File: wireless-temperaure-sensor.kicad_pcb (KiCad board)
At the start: 2 copper layers, 45.1 x 55.9 mm, 18 parts, among them J1 Programmer, U1 stm32l010f4, U2 NRF24L01_Breakout, U3 MCP9808_MSOP

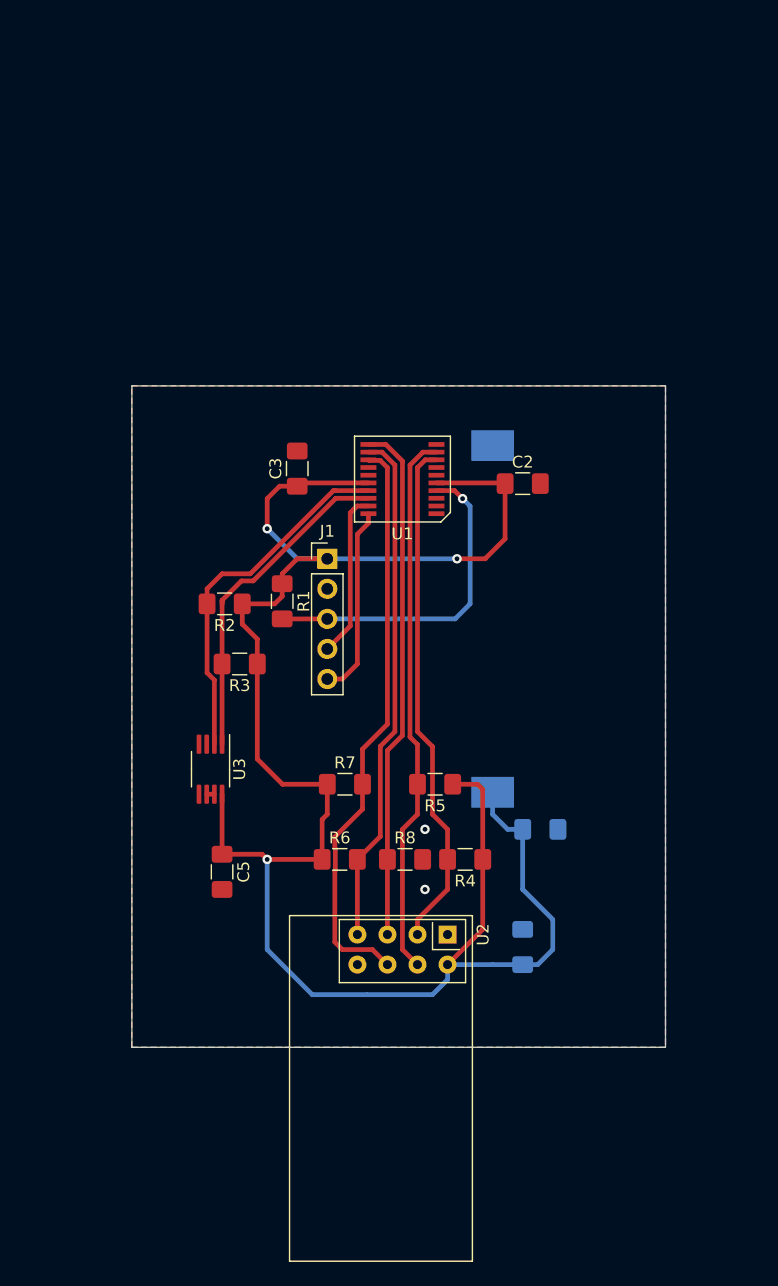
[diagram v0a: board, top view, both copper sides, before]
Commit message: Finished schematic and almost finished pcb
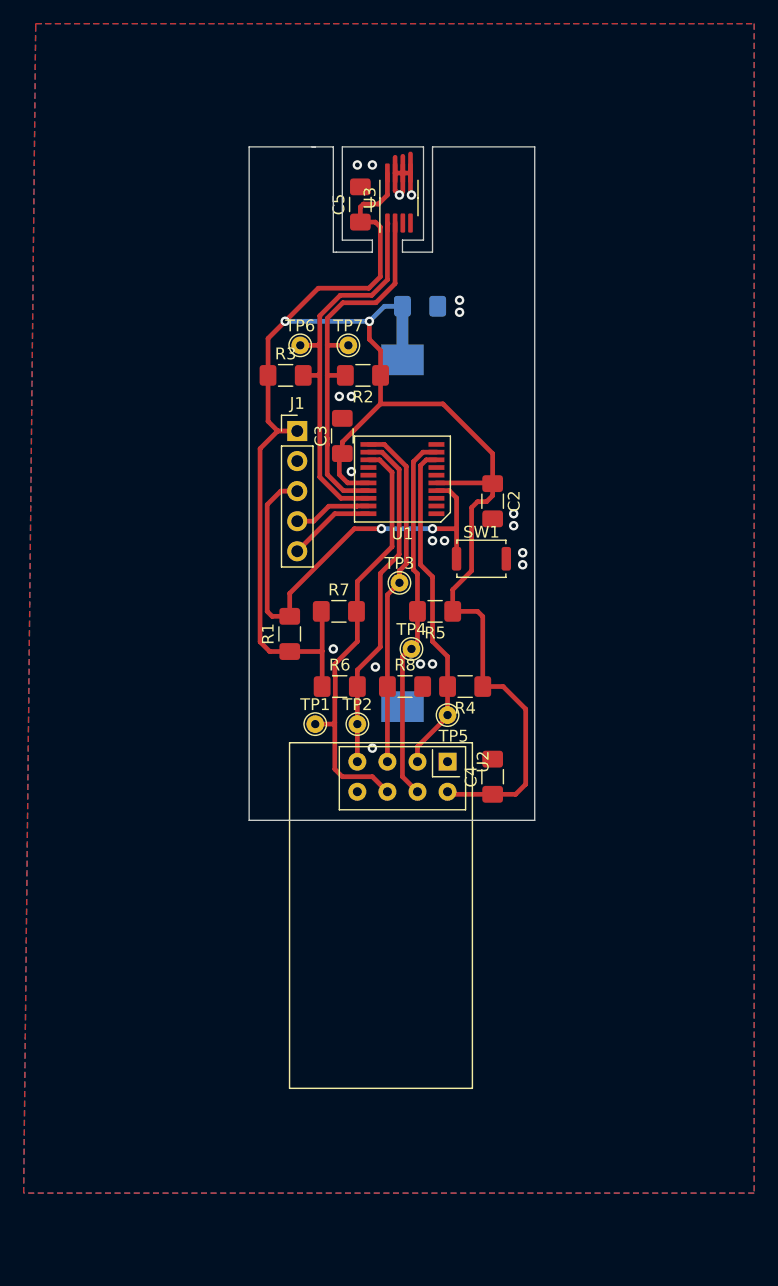
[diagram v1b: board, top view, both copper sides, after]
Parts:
- added SW1: SW_Push, Button_Switch_SMD:SW_Push_SPST_NO_Alps_SKRK, F.Cu at (105.7, 92.7)
- added TP1: , TestPoint:TestPoint_THTPad_D1.5mm_Drill0.7mm, F.Cu at (91.7, 106.7)
- added TP2: , TestPoint:TestPoint_THTPad_D1.5mm_Drill0.7mm, F.Cu at (95.2, 106.7)
- added TP3: , TestPoint:TestPoint_THTPad_D1.5mm_Drill0.7mm, F.Cu at (98.8, 94.7)
- added TP4: , TestPoint:TestPoint_THTPad_D1.5mm_Drill0.7mm, F.Cu at (99.8, 100.3)
- added TP5: , TestPoint:TestPoint_THTPad_D1.5mm_Drill0.7mm, F.Cu at (102.9, 105.9)
- added TP6: , TestPoint:TestPoint_THTPad_D1.5mm_Drill0.7mm, F.Cu at (90.4, 74.7)
- added TP7: , TestPoint:TestPoint_THTPad_D1.5mm_Drill0.7mm, F.Cu at (94.5, 74.7)
- C4: moved to F.Cu
- moved C5 57.6 mm to (95.5, 62.8), turned to 90 degrees
- moved U3 50.8 mm to (98.8, 62.2), turned to 90 degrees
- moved C1 45.3 mm to (100.5, 71.4)
- moved R3 24.7 mm to (89.2, 77.2), turned to 0 degrees
- moved R2 22.6 mm to (95.7, 77.2)
- moved R7 14.6 mm to (93.7, 97.2)
- moved C4 14.6 mm to (106.7, 111.1)
- moved R4 14.6 mm to (104.4, 103.5)
- moved R5 14.6 mm to (101.8, 97.2)
- moved R6 14.6 mm to (93.8, 103.5)
- moved R8 14.6 mm to (99.3, 103.5)
- moved U2 14.6 mm to (102.9, 109.9)
- moved J1 11.1 mm to (90.2, 81.9)
- moved BT1 10.5 mm to (99.1, 90.6), turned to 270 degrees
- moved C3 4.70 mm to (94.0, 82.3)
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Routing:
- net /NRF_CE: track 43.4 -> 28.6 mm
- net /NCSN: track 46.2 -> 31.4 mm
- net /SPI_SCK: track 44.0 -> 29.6 mm
- net /MISO: track 43.7 -> 29.4 mm
- net /MOSI: track 49.1 -> 36.5 mm
- net /NRST: track 28.0 -> 39.5 mm, vias 1 -> 2
- net VDD: track 164.8 -> 153.9 mm, vias 3 -> 2
- net GND: track 0.65 -> 11.5 mm, vias 2 -> 20
- net /SWCLK: track 16.2 -> 7.33 mm
- net /SWDIO: track 14.1 -> 6.55 mm
- net /SDA: track 28.4 -> 33.5 mm
- net /SCL: track 30.5 -> 32.4 mm
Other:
- board size 45.1 x 55.9 mm -> 24.1 x 56.9 mm

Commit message: Added gerber and drill files#
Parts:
- renumbered TP5 to CE, TP4 to CSN, TP2 to MISO, TP1 to MOSI, TP3 to SCK
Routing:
- net GND: track 11.5 -> 14.2 mm, vias 20 -> 34
- net /NRF_CE: track 28.6 -> 29.1 mm
- net /NCSN: track 31.4 -> 31.9 mm
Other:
- outline, holes or cut-outs redrawn
